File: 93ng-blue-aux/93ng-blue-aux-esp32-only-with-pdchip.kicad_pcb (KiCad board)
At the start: 2 copper layers, 50 x 50 mm, 38 parts, among them J1 12V INPUT, J2 ESP32 UART, J3 USB_C_Receptacle_USB2.0, J7 I-BUS, Q1 S8050, Q2 S8050, SW1 PWR IN SELECT, U1 ESP32-WROOM-32D, U2 NCP1117-3.3_SOT223, U3 MC33897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

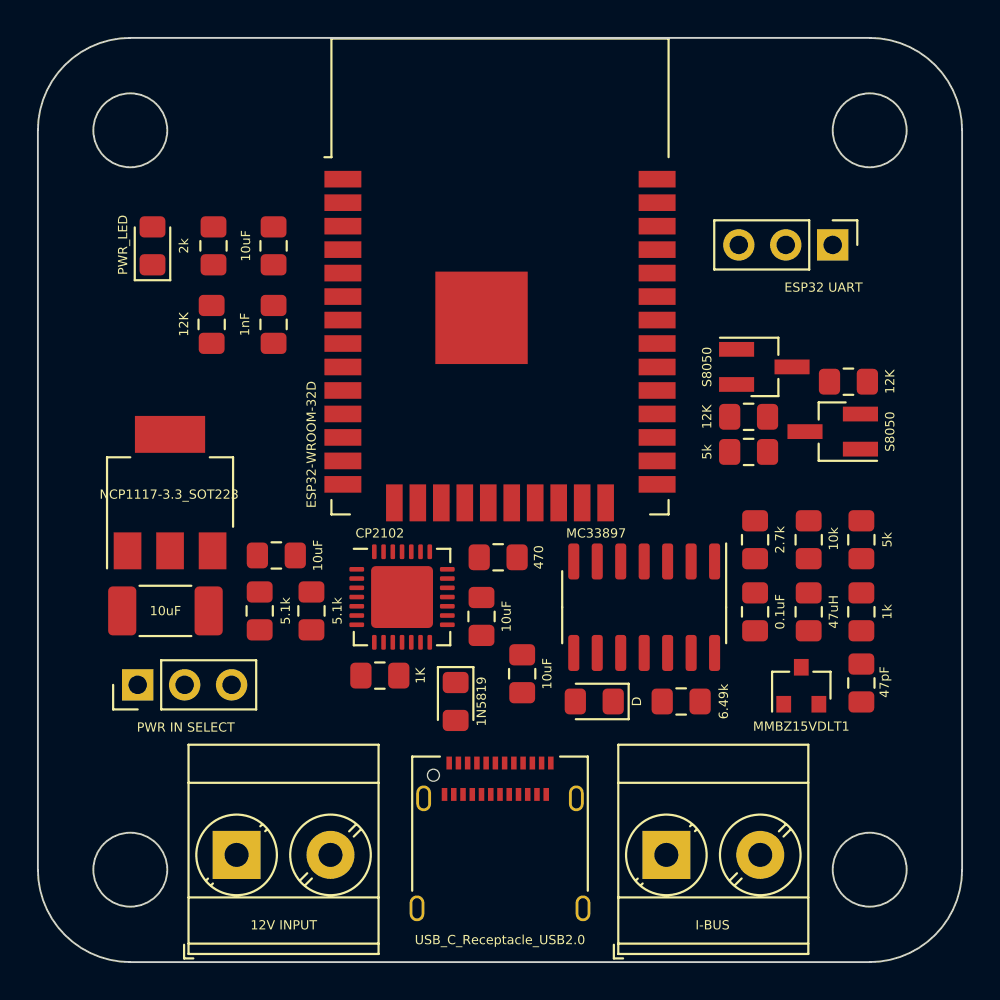
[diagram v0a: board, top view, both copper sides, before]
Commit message: Made new version without USBC-PD chip, and simple pulldowns. Placement looks good.
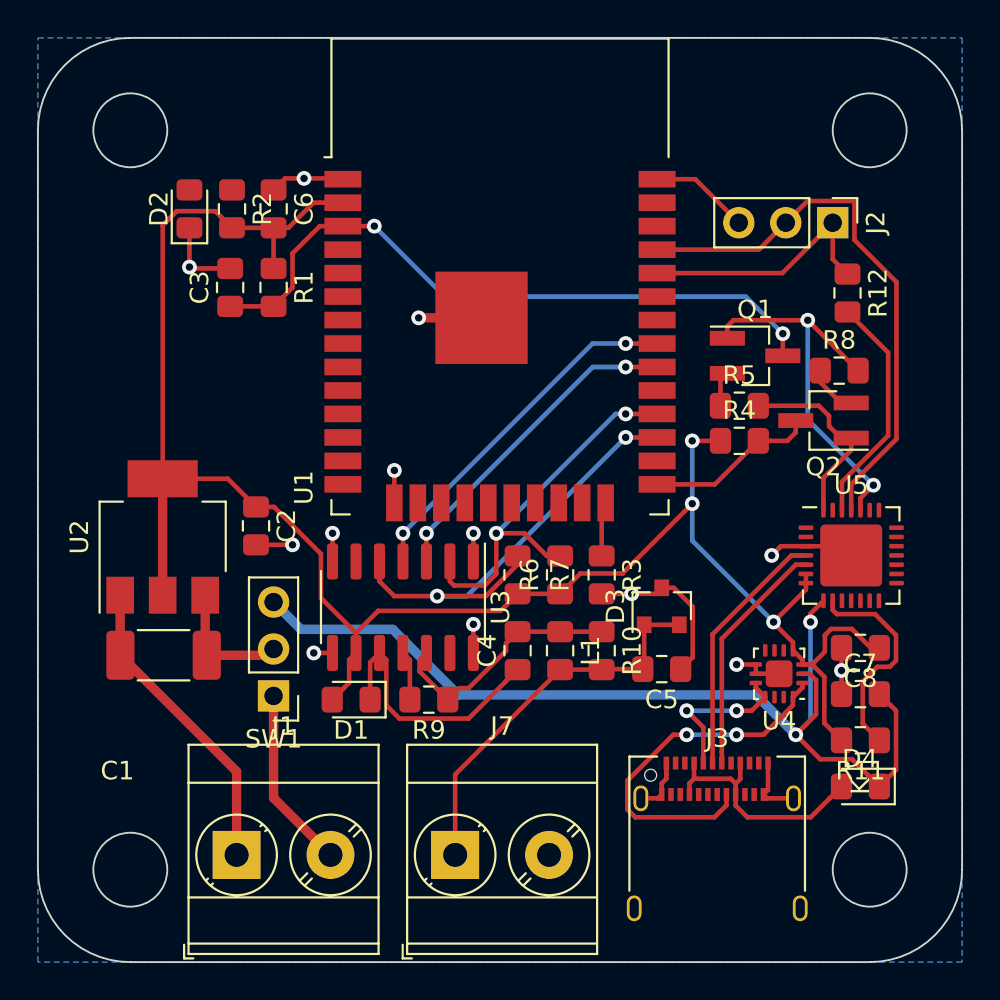
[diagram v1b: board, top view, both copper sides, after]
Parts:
- removed R13, R14: 5.1k, Resistor_SMD:R_0805_2012Metric_Pad1.15x1.40mm_HandSolder
- added U4: FUSB302BMPX, Package_DFN_QFN:WQFN-14-1EP_2.5x2.5mm_P0.5mm_EP1.45x1.45mm, F.Cu at (210.1, 106.4)
- U5: value CP2102 -> CP2102N-A01-GQFN28
- moved R11 26.2 mm to (214.5, 110.0)
- moved U5 24.4 mm to (214.0, 100.0)
- moved R12 23.7 mm to (213.8, 85.8), turned to 270 degrees
- moved D4 22.4 mm to (214.5, 112.5), turned to 180 degrees
- moved C7 20.9 mm to (214.5, 107.5), turned to 0 degrees
- moved C8 18.4 mm to (214.5, 105.0), turned to 180 degrees
- moved R10 14.2 mm to (200.5, 105.2)
- moved R3 14.2 mm to (200.5, 101.0)
- moved R9 13.7 mm to (191.2, 107.8)
- moved L1 13.6 mm to (198.2, 105.2)
- moved R6 13.6 mm to (198.2, 101.0)
- moved D1 13.2 mm to (186.9, 107.8)
- moved U3 13.1 mm to (189.8, 102.8)
- moved C4 13.0 mm to (195.9, 105.2)
- moved R7 13.0 mm to (195.9, 101.0)
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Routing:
- net 3.3V: track 0.00 -> 103.9 mm, vias 0 -> 3
- net GND: track 0.00 -> 68.9 mm, vias 0 -> 13
- net USB_VBUS: track 0.00 -> 54.8 mm, vias 0 -> 2
- net ESP32_EN: track 0.00 -> 36.4 mm, vias 0 -> 2
- net ESP32_TX: track 0.00 -> 30.4 mm
- net MC33_RX: track 0.00 -> 25.5 mm, vias 0 -> 2
- net MC33_TX: track 0.00 -> 21.5 mm, vias 0 -> 2
- net SW_CAN: track 0.00 -> 21.2 mm
- net RTS: track 0.00 -> 21.0 mm, vias 0 -> 2
- net USB_CC2: track 0.00 -> 20.0 mm, vias 0 -> 2
- net MC33_MODE1: track 0.00 -> 19.5 mm, vias 0 -> 2
- net MC33_MODE0: track 0.00 -> 17.7 mm, vias 0 -> 2
- net Net-(C4-Pad1): track 0.00 -> 14.2 mm
- net USB_D+: track 0.00 -> 13.8 mm
- net ESP32_RX: track 0.00 -> 13.7 mm
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- added copper zone on B.Cu, net GND
